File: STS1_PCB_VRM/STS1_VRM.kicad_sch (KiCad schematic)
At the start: 16 parts

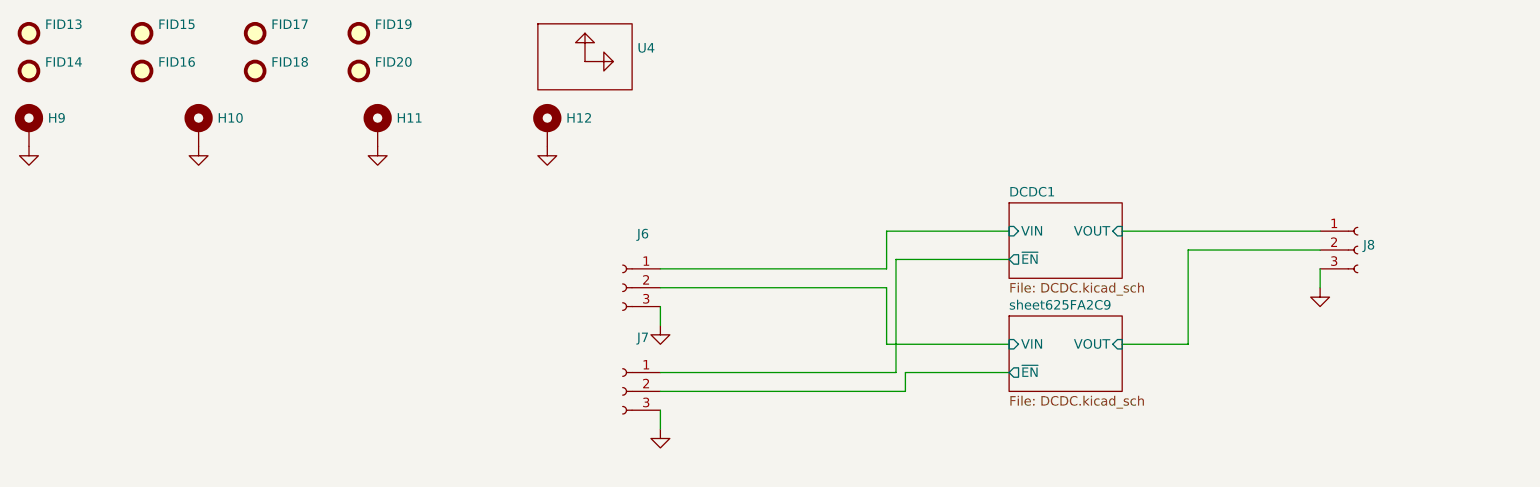
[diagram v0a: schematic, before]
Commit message: more work done
All parts besides RF added
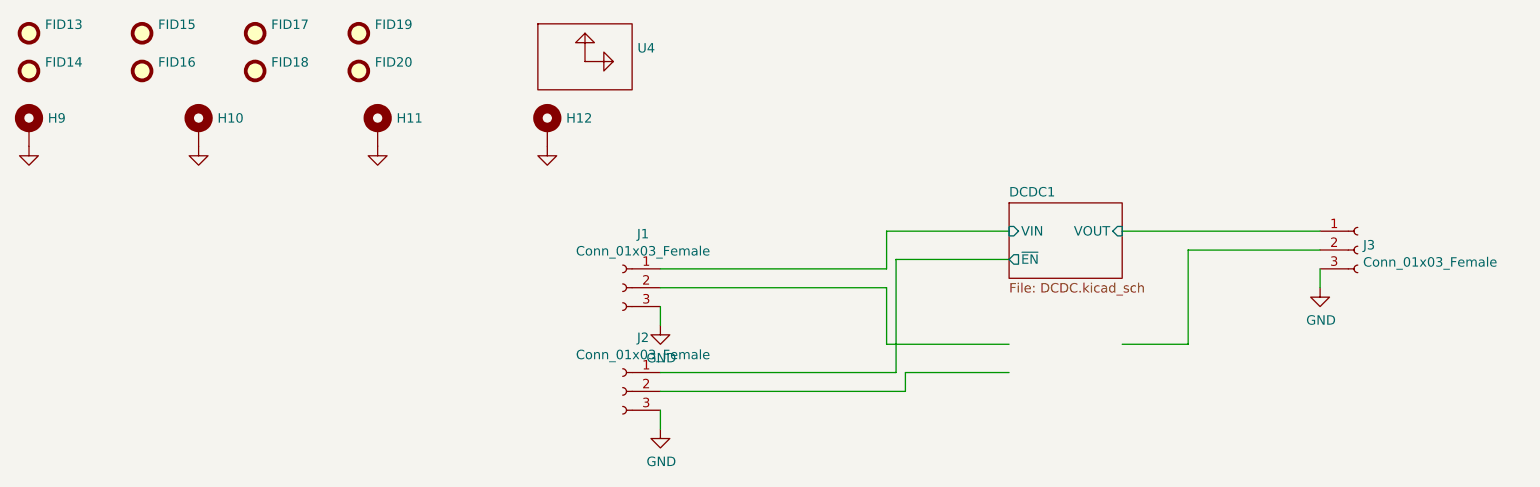
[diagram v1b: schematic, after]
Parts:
- FID13, FID14, FID15, FID16, FID17, FID18, FID19, FID20, H10, H11, H12, H9, U4: value (none) -> ~
- J1: renamed from J6; value (none) -> Conn_01x03_Female; footprint (none) -> Connector_PinHeader_2.54mm:PinHeader_1x03_P2.54mm_Vertical
- J2: renamed from J7; value (none) -> Conn_01x03_Female; footprint (none) -> Connector_PinHeader_2.54mm:PinHeader_1x03_P2.54mm_Vertical
- J3: renamed from J8; value (none) -> Conn_01x03_Female; footprint (none) -> Connector_PinHeader_2.54mm:PinHeader_1x03_P2.54mm_Vertical
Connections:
- net sheet625FA2C9/VIN: no longer names the net of J1.2 (Pin_2)
- net sheet625FA2C9/VOUT: no longer names the net of J3.2 (Pin_2)
- net sheet625FA2C9/~{EN}: no longer names the net of J2.2 (Pin_2)
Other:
- removed sheet sheet625FA2C9
